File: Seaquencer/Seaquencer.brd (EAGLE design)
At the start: 94.9 x 72.4 mm, 43 parts, among them IC2 74HC595N, SW2 EC12E_SW

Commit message: Sequencer: POT追加前（完成形）
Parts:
- removed R1: (no value), rcl:0207/7
- removed SW2: EC12E_SW, switch-alps:ALPS_EC12E_SW
- added JP4: RE_AB, pinhead:1X03
- added JP5: RE_SW, pinhead:1X03
- moved R11 15.5 mm to (86.4, 39.4)
- moved R2 15.5 mm to (19.1, 63.5)
- moved R12 15.5 mm to (88.9, 39.4)
- moved LED1 12.7 mm to (15.2, 67.3)
- moved JP1 5.08 mm to (41.9, 68.6)
- moved JP2 2.54 mm to (50.8, 68.6)
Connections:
- removed net N$10: ATMEGA88.27, JP2.3
- removed net N$14: IC2.10, R1.1
- removed net N$37: ATMEGA88.23, SW2.A
- removed net N$38: ATMEGA88.24, SW2.B
- removed net N$8: ATMEGA88.25, SW2.D
- new net N$42: ATMEGA88.1, JP2.3
- new net RE_A: ATMEGA88.18, JP4.3
- new net RE_B: ATMEGA88.19, JP4.1
- new net RE_S: ATMEGA88.17, JP5.3
- net +3V3: now also IC2.10; no longer R1.2
- net GND: now also JP5.1; no longer SW2.C, SW2.E
- net N$11: now also ATMEGA88.23; no longer ATMEGA88.15
- net N$12: now also ATMEGA88.24; no longer ATMEGA88.17
- net N$32: now also ATMEGA88.25; no longer ATMEGA88.16
- net N$35: now also ATMEGA88.16; no longer ATMEGA88.19
- net N$36: now also ATMEGA88.15; no longer ATMEGA88.18
- net N$39: now also ATMEGA88.27, JP2.2; no longer ATMEGA88.1, JP2.1
- net N$9: now also JP2.1; no longer JP2.2
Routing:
- net RE_S: track 0.00 -> 111.8 mm
- net RE_A: track 0.00 -> 86.4 mm
- net RE_B: track 0.00 -> 76.2 mm
- net N$11: track 0.00 -> 48.3 mm
- net N$12: track 0.00 -> 38.1 mm
- net N$32: track 0.00 -> 30.5 mm
- net N$36: track 36.6 -> 7.62 mm
- net N$35: track 46.8 -> 17.8 mm
- net N$39: track 0.00 -> 22.9 mm
- net N$10: track 22.9 -> 0.00 mm
- net N$33: track 0.00 -> 18.8 mm
- net +3V3: track 83.4 -> 101.6 mm
- net N$34: track 0.00 -> 17.8 mm
- net GND: track 342.1 -> 349.2 mm
- net N$30: track 0.00 -> 2.54 mm
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
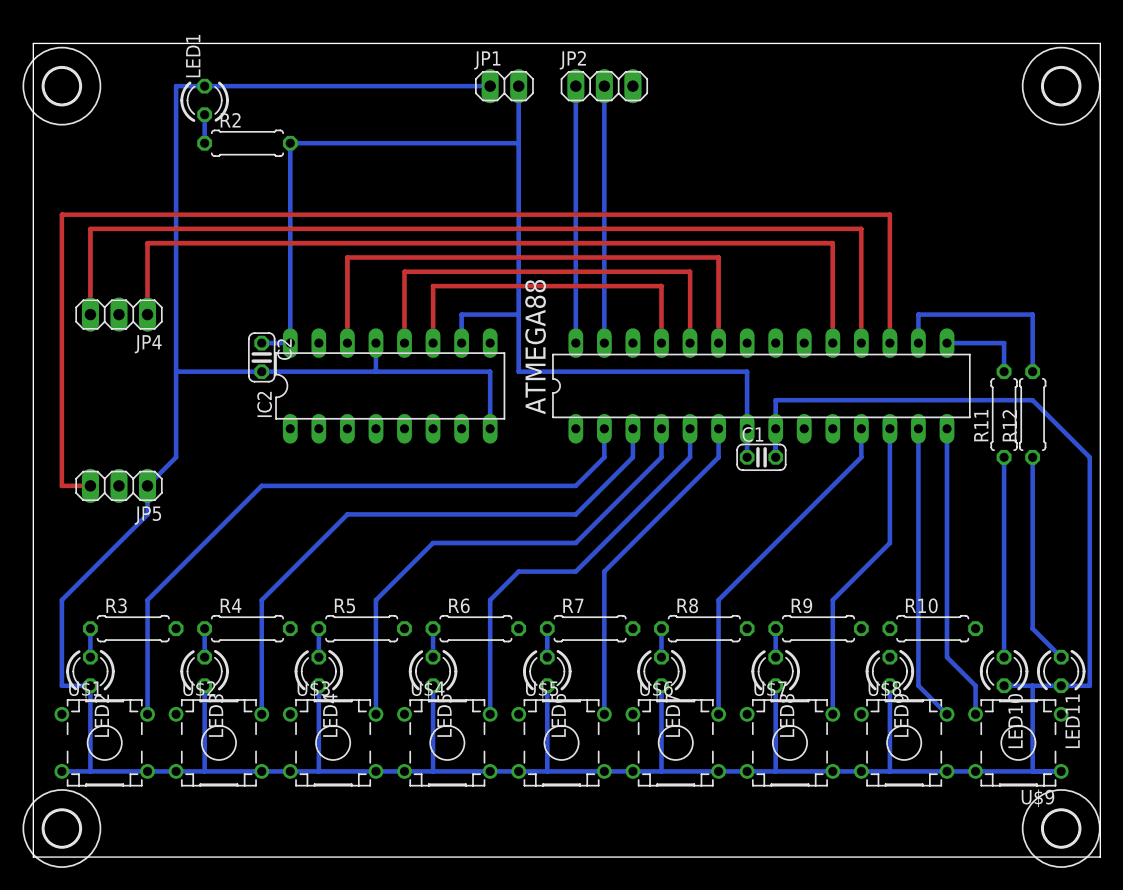
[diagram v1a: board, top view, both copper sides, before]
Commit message: Sequencer: POTを追加
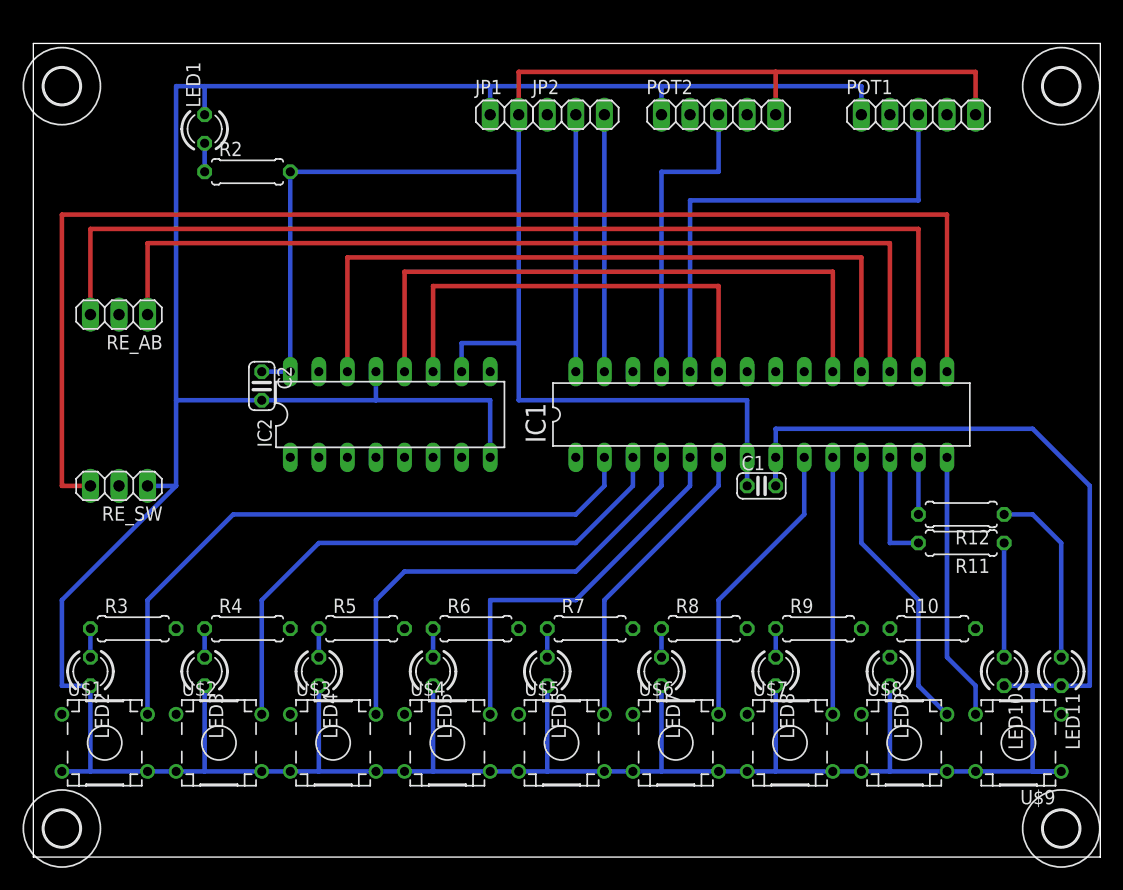
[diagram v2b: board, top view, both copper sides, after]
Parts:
- removed ATMEGA88: ATMEGA48/88/168, mylib:DIL28-3
- added IC1: ATMEGA48/88/168, mylib:DIL28-3
- added POT1, POT2: (no value), pinhead:1X05
- RE_AB: value RE_AB -> (none)
- RE_SW: value RE_SW -> (none)
- moved R11 12.0 mm to (82.5, 27.9), turned to 180 degrees
- moved R12 10.9 mm to (82.5, 30.5), turned to 180 degrees
- moved JP2 3.59 mm to (48.3, 66.0)
- moved C2 2.54 mm to (20.3, 41.9)
- moved LED1 2.54 mm to (15.2, 64.8)
- moved C1 2.54 mm to (64.8, 33.0)
- moved IC2 2.54 mm to (31.8, 39.4)
- moved R2 2.54 mm to (19.1, 61.0)
- moved JP1 2.54 mm to (41.9, 66.0)
- renumbered JP4 to RE_AB, JP5 to RE_SW
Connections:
- removed net N$32: ATMEGA88.25, IC2.11
- removed net N$39: ATMEGA88.27, JP2.2
- removed net N$42: ATMEGA88.1, JP2.3
- new net N$10: IC1.24, POT1.3
- new net N$8: IC1.18, IC2.14
- new net RST: IC1.1, JP2.1
- new net SCL: IC1.28, JP2.2
- new net SDA: IC1.27, JP2.3
- net +3V3: now also IC1.7, POT1.5, POT2.5; no longer ATMEGA88.7
- net AVCC: now also IC1.20; no longer ATMEGA88.20
- net GND: now also IC1.8, POT1.1, POT2.1; no longer ATMEGA88.8
- net GND2: now also IC1.22; no longer ATMEGA88.22
- net N$1: now also IC1.2; no longer ATMEGA88.2
- net N$11: now also IC1.25, POT2.3; no longer ATMEGA88.23, IC2.14
- net N$12: now also IC1.19; no longer ATMEGA88.24
- net N$13: now also IC1.14; no longer ATMEGA88.14
- net N$2: now also IC1.3; no longer ATMEGA88.3
- net N$3: now also IC1.11; no longer ATMEGA88.13
- net N$35: now also IC1.13; no longer ATMEGA88.16
- net N$36: now also IC1.12; no longer ATMEGA88.15
- net N$4: now also IC1.10; no longer ATMEGA88.12
- net N$41: now also IC1.4; no longer ATMEGA88.4
- net N$5: now also IC1.9; no longer ATMEGA88.11
- net N$6: now also IC1.6; no longer ATMEGA88.6
- net N$7: now also IC1.5; no longer ATMEGA88.5
- net N$9: now also IC1.23, IC2.11; no longer ATMEGA88.28, JP2.1
- net RE_A: now also IC1.16; no longer ATMEGA88.18
- net RE_B: now also IC1.17; no longer ATMEGA88.19
- net RE_S: now also IC1.15; no longer ATMEGA88.17
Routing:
- net N$8: track 0.00 -> 66.0 mm
- net +3V3: track 101.6 -> 153.7 mm
- net N$10: track 0.00 -> 43.2 mm
- net GND: track 349.2 -> 392.4 mm
- net N$32: track 30.5 -> 0.00 mm
- net SDA: track 0.00 -> 22.9 mm
- net SCL: track 0.00 -> 22.9 mm
- net N$39: track 22.9 -> 0.00 mm
- net N$11: track 48.3 -> 27.9 mm
- net N$12: track 38.1 -> 55.9 mm
- net N$9: track 22.9 -> 40.6 mm
- net N$35: track 17.8 -> 5.08 mm
- net RE_B: track 76.2 -> 83.8 mm
- net N$34: track 17.8 -> 10.2 mm
- net RE_S: track 111.8 -> 119.4 mm
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
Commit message: Sequencer: Add Jumper
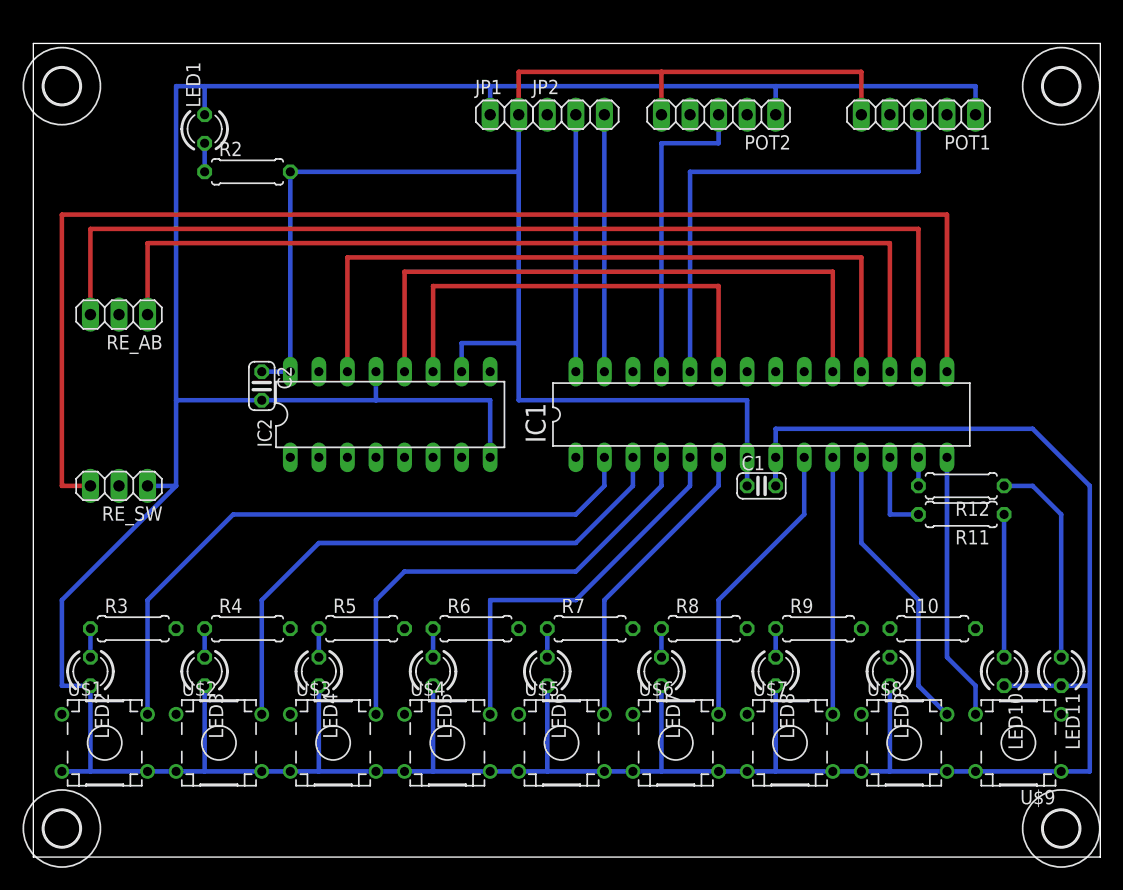
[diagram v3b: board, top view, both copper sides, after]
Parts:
- moved R12 2.54 mm to (82.5, 33.0)
- moved R11 2.54 mm to (82.5, 30.5)
- turned POT1 to 180 degrees
- turned POT2 to 180 degrees
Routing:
- net GND: track 392.4 -> 402.6 mm
- net +3V3: track 153.7 -> 143.5 mm
- net N$35: track 5.08 -> 2.54 mm
- net N$36: track 10.2 -> 7.62 mm
- net N$34: track 10.2 -> 12.7 mm
- net N$33: track 16.3 -> 18.8 mm
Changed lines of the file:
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@@
 <layer number="97" name="Info" color="7" fill="1" visible="no" active="no"/>
 <layer number="98" name="Guide" color="6" fill="1" visible="no" active="no"/>
-<layer number="100" name="Grid" color="11" fill="1" visible="yes" active="yes"/>
+<layer number="100" name="Grid" color="11" fill="1" visible="no" active="yes"/>
+<layer number="101" name="Jumper" color="14" fill="1" visible="yes" active="yes"/>
 <layer number="200" name="200bmp" color="1" fill="10" visible="no" active="no"/>
 <layer number="201" name="tNamesOnPCB" color="5" fill="1" visible="yes" active="yes"/>
@@
 <wire x1="76.2" y1="0" x2="76.2" y2="68.58" width="0" layer="100"/>
 <wire x1="88.9" y1="0" x2="88.9" y2="68.58" width="0" layer="100"/>
+<wire x1="12.7" y1="20.32" x2="25.4" y2="43.18" width="0.4064" layer="101"/>
+<wire x1="22.86" y1="35.56" x2="22.86" y2="20.32" width="0.4064" layer="101"/>
+<wire x1="25.4" y1="35.56" x2="33.02" y2="20.32" width="0.4064" layer="101"/>
+<wire x1="27.94" y1="35.56" x2="43.18" y2="20.32" width="0.4064" layer="101"/>
+<wire x1="30.48" y1="35.56" x2="53.34" y2="20.32" width="0.4064" layer="101"/>
+<wire x1="33.02" y1="35.56" x2="63.5" y2="20.32" width="0.4064" layer="101"/>
+<wire x1="35.56" y1="35.56" x2="73.66" y2="20.32" width="0.4064" layer="101"/>
+<wire x1="38.1" y1="35.56" x2="83.82" y2="20.32" width="0.4064" layer="101"/>
+<wire x1="45.72" y1="66.04" x2="48.26" y2="35.56" width="0.4064" layer="101"/>
 </plain>
 <attributes>
@@
 <element name="LED8" library="led" package="LED3MM" value="" x="66.04" y="16.51" rot="R270"/>
 <element name="LED9" library="led" package="LED3MM" value="" x="76.2" y="16.51" rot="R270"/>
-<element name="R11" library="rcl" package="0207/7" value="" x="82.55" y="27.94" rot="R180"/>
-<element name="R12" library="rcl" package="0207/7" value="" x="82.55" y="30.48" rot="R180"/>
+<element name="R11" library="rcl" package="0207/7" value="" x="82.55" y="30.48" rot="R180"/>
+<element name="R12" library="rcl" package="0207/7" value="" x="82.55" y="33.02" rot="R180"/>
 <element name="LED10" library="led" package="LED3MM" value="" x="86.36" y="16.51" rot="R270"/>
 <element name="LED11" library="led" package="LED3MM" value="" x="91.44" y="16.51" rot="R270"/>
@@
 <element name="RE_SW" library="pinhead" package="1X03" value="" x="7.62" y="33.02" rot="R180"/>
 <element name="JP2" library="pinhead" package="1X03" value="I2C" x="48.26" y="66.04"/>
-<element name="POT1" library="pinhead" package="1X05" value="" x="78.74" y="66.04"/>
-<element name="POT2" library="pinhead" package="1X05" value="" x="60.96" y="66.04"/>
+<element name="POT1" library="pinhead" package="1X05" value="" x="78.74" y="66.04" rot="R180"/>
+<element name="POT2" library="pinhead" package="1X05" value="" x="60.96" y="66.04" rot="R180"/>
 </elements>
 <signals>
@@
 <contactref element="U$9" pad="6"/>
 <wire x1="81.28" y1="7.62" x2="83.82" y2="7.62" width="0.4064" layer="16"/>
-<wire x1="83.82" y1="7.62" x2="91.44" y2="7.62" width="0.4064" layer="16"/>
-<wire x1="86.36" y1="15.24" x2="88.9" y2="15.24" width="0.4064" layer="16"/>
 <contactref element="IC1" pad="8"/>
 <contactref element="C1" pad="2"/>
-<wire x1="88.9" y1="15.24" x2="91.44" y2="15.24" width="0.4064" layer="16"/>
+<wire x1="86.36" y1="15.24" x2="91.44" y2="15.24" width="0.4064" layer="16"/>
 <wire x1="40.64" y1="40.64" x2="40.64" y2="35.56" width="0.4064" layer="16"/>
 <wire x1="66.04" y1="35.56" x2="66.04" y2="33.02" width="0.4064" layer="16"/>
 <contactref element="RE_SW" pad="1"/>
-<wire x1="91.44" y1="7.62" x2="88.9" y2="7.62" width="0.4064" layer="16"/>
-<wire x1="88.9" y1="7.62" x2="88.9" y2="15.24" width="0.4064" layer="16"/>
+<wire x1="93.98" y1="7.62" x2="83.82" y2="7.62" width="0.4064" layer="16"/>
 <wire x1="66.04" y1="33.02" x2="66.04" y2="38.1" width="0.4064" layer="16"/>
 <wire x1="66.04" y1="38.1" x2="88.9" y2="38.1" width="0.4064" layer="16"/>
@@
 <contactref element="POT1" pad="1"/>
 <contactref element="POT2" pad="1"/>
-<wire x1="55.88" y1="68.58" x2="73.66" y2="68.58" width="0.4064" layer="16"/>
-<wire x1="73.66" y1="68.58" x2="73.66" y2="66.04" width="0.4064" layer="16"/>
-<wire x1="55.88" y1="66.04" x2="55.88" y2="68.58" width="0.4064" layer="16"/>
-<wire x1="55.88" y1="68.58" x2="40.64" y2="68.58" width="0.4064" layer="16"/>
+<wire x1="40.64" y1="68.58" x2="66.04" y2="68.58" width="0.4064" layer="16"/>
+<wire x1="66.04" y1="68.58" x2="83.82" y2="68.58" width="0.4064" layer="16"/>
+<wire x1="93.98" y1="7.62" x2="93.98" y2="15.24" width="0.4064" layer="16"/>
+<wire x1="83.82" y1="66.04" x2="83.82" y2="68.58" width="0.4064" layer="16"/>
+<wire x1="66.04" y1="66.04" x2="66.04" y2="68.58" width="0.4064" layer="16"/>
+<wire x1="93.98" y1="7.62" x2="91.44" y2="7.62" width="0" layer="19" extent="16-16"/>
 </signal>
 <signal name="N$1">
@@
 <contactref element="POT2" pad="5"/>
 <wire x1="43.18" y1="66.04" x2="43.18" y2="69.85" width="0.4064" layer="1"/>
-<wire x1="43.18" y1="69.85" x2="66.04" y2="69.85" width="0.4064" layer="1"/>
-<wire x1="66.04" y1="69.85" x2="83.82" y2="69.85" width="0.4064" layer="1"/>
-<wire x1="83.82" y1="69.85" x2="83.82" y2="66.04" width="0.4064" layer="1"/>
-<wire x1="66.04" y1="66.04" x2="66.04" y2="69.85" width="0.4064" layer="1"/>
+<wire x1="43.18" y1="69.85" x2="55.88" y2="69.85" width="0.4064" layer="1"/>
+<wire x1="55.88" y1="69.85" x2="73.66" y2="69.85" width="0.4064" layer="1"/>
+<wire x1="55.88" y1="66.04" x2="55.88" y2="69.85" width="0.4064" layer="1"/>
+<wire x1="73.66" y1="66.04" x2="73.66" y2="69.85" width="0.4064" layer="1"/>
 </signal>
 <signal name="N$15">
@@
 <contactref element="LED11" pad="A"/>
 <contactref element="R12" pad="1"/>
-<wire x1="86.36" y1="30.48" x2="88.9" y2="30.48" width="0.4064" layer="16"/>
-<wire x1="88.9" y1="30.48" x2="91.44" y2="27.94" width="0.4064" layer="16"/>
-<wire x1="91.44" y1="27.94" x2="91.44" y2="17.78" width="0.4064" layer="16"/>
+<wire x1="91.44" y1="30.48" x2="91.44" y2="17.78" width="0.4064" layer="16"/>
+<wire x1="86.36" y1="33.02" x2="88.9" y2="33.02" width="0.4064" layer="16"/>
+<wire x1="88.9" y1="33.02" x2="91.44" y2="30.48" width="0.4064" layer="16"/>
 </signal>
 <signal name="N$34">
 <contactref element="LED10" pad="A"/>
 <contactref element="R11" pad="1"/>
-<wire x1="86.36" y1="27.94" x2="86.36" y2="17.78" width="0.4064" layer="16"/>
+<wire x1="86.36" y1="30.48" x2="86.36" y2="17.78" width="0.4064" layer="16"/>
 </signal>
 <signal name="N$36">
 <contactref element="R11" pad="2"/>
 <contactref element="IC1" pad="12"/>
-<wire x1="76.2" y1="35.56" x2="76.2" y2="27.94" width="0.4064" layer="16"/>
-<wire x1="76.2" y1="27.94" x2="78.74" y2="27.94" width="0.4064" layer="16"/>
+<wire x1="76.2" y1="35.56" x2="76.2" y2="30.48" width="0.4064" layer="16"/>
+<wire x1="76.2" y1="30.48" x2="78.74" y2="30.48" width="0.4064" layer="16"/>
 </signal>
 <signal name="N$12">
@@
 <contactref element="R12" pad="2"/>
 <contactref element="IC1" pad="13"/>
-<wire x1="78.74" y1="35.56" x2="78.74" y2="30.48" width="0.4064" layer="16"/>
+<wire x1="78.74" y1="35.56" x2="78.74" y2="33.02" width="0.4064" layer="16"/>
 </signal>
 <signal name="SCL">
@@
 <signal name="N$10">
 <contactref element="IC1" pad="24"/>
-<wire x1="58.42" y1="43.18" x2="58.42" y2="58.42" width="0.4064" layer="16"/>
+<wire x1="58.42" y1="43.18" x2="58.42" y2="60.96" width="0.4064" layer="16"/>
 <contactref element="POT1" pad="3"/>
-<wire x1="58.42" y1="58.42" x2="78.74" y2="58.42" width="0.4064" layer="16"/>
-<wire x1="78.74" y1="58.42" x2="78.74" y2="66.04" width="0.4064" layer="16"/>
+<wire x1="58.42" y1="60.96" x2="78.74" y2="60.96" width="0.4064" layer="16"/>
+<wire x1="78.74" y1="60.96" x2="78.74" y2="66.04" width="0.4064" layer="16"/>
 </signal>
 <signal name="N$11">
 <contactref element="IC1" pad="25"/>
-<wire x1="55.88" y1="43.18" x2="55.88" y2="60.96" width="0.4064" layer="16"/>
+<wire x1="55.88" y1="43.18" x2="55.88" y2="63.5" width="0.4064" layer="16"/>
 <contactref element="POT2" pad="3"/>
-<wire x1="55.88" y1="60.96" x2="60.96" y2="60.96" width="0.4064" layer="16"/>
-<wire x1="60.96" y1="60.96" x2="60.96" y2="66.04" width="0.4064" layer="16"/>
+<wire x1="60.96" y1="63.5" x2="60.96" y2="66.04" width="0.4064" layer="16"/>
+<wire x1="55.88" y1="63.5" x2="60.96" y2="63.5" width="0.4064" layer="16"/>
 </signal>
 </signals>
